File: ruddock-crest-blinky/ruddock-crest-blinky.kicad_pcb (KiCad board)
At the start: 2 copper layers, 38.1 x 45.7 mm, 38 parts, among them J1 JST PH, Q1 IRFML8244, SW1 JS102011JCQN, SW2 PTS 647 SK38 SMTR2 LFS, U1 ATtiny85-20SU, U2 74HC595

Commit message: Begin layout
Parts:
- removed the G*** at (141.0, 108.2)
- removed H1: BAT_POS, TestPoint:TestPoint_Pad_4.0x4.0mm
- removed H2: BAT_NEG, TestPoint:TestPoint_Pad_4.0x4.0mm
- removed the R1 at (108.5, 105.3)
- added BT1: 3024, Battery:BatteryHolder_Keystone_3034_1x20mm, B.Cu at (212.1, 79.0)
- added C5: 1uF, Capacitor_SMD:C_0805_2012Metric_Pad1.15x1.40mm_HandSolder, B.Cu at (198.1, 59.4)
- added R10: 10K, Resistor_SMD:R_0805_2012Metric_Pad1.15x1.40mm_HandSolder, B.Cu at (207.5, 54.6)
- added R9: 10K, Resistor_SMD:R_0805_2012Metric_Pad1.15x1.40mm_HandSolder, B.Cu at (201.9, 67.3)
- added U3: AP7370-50, Package_TO_SOT_SMD:SOT-89-3_Handsoldering, B.Cu at (194.3, 63.2)
- C1, C2, C3, C4, F1, J1, Q1, SW2, U1, U2: moved to B.Cu
- C6: renamed from C5; value 1uF -> 0.1uF; moved to B.Cu
- moved J1 134.7 mm to (212.1, 85.1), turned to 0 degrees
- moved Q1 134.2 mm to (226.1, 71.1), turned to 90 degrees
- moved C1 123.1 mm to (204.0, 54.6), turned to 90 degrees
- moved SW2 118.2 mm to (176.5, 55.9)
- moved U1 114.2 mm to (205.7, 61.0)
- moved U2 113.4 mm to (217.2, 59.7)
- moved C2 111.3 mm to (210.8, 54.6), turned to 90 degrees
- moved C6 106.6 mm to (200.7, 54.6), turned to 90 degrees
- moved F1 98.4 mm to (196.8, 79.0), turned to 90 degrees
- moved C4 94.8 mm to (193.8, 69.4)
- moved C3 86.7 mm to (193.8, 72.9)
- moved G*** 52.2 mm to (106.7, 147.3)
- moved G*** 43.2 mm to (184.2, 106.7)
- moved R11 4.72 mm to (129.8, 74.5)
- renumbered R2 to R1, R10 to R11, R3 to R2, R4 to R3, R5 to R4, R6 to R5, R7 to R6, R8 to R7, R9 to R8
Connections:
- net Net-(R2-Pad1) renamed /LED1
- net Net-(R3-Pad1) renamed /LED2
- net Net-(R4-Pad1) renamed /LED3
- net Net-(R5-Pad1) renamed /LED4
- net Net-(R6-Pad1) renamed /LED5
- net Net-(R7-Pad1) renamed /LED6
- net Net-(R8-Pad1) renamed /LED7
- net Net-(R9-Pad1) renamed /LED8
- C1 pad 1: VCC -> VDD
- C2 pad 1: GND -> VDD
- C2 pad 2: VCC -> GND
- C3 pad 1: VCC -> +BATT
- C4 pad 1: VCC -> +BATT
- Q1 pad 1: VCC -> +BATT
- R11 pad 1: VCC -> VDD
- SW1 pad 2: VCC -> +BATT
- U1 pad 8: VCC -> VDD
- U2 pad 10: VCC -> VDD
- U2 pad 16: VCC -> VDD
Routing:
- net Net-(R2-Pad2): track 21.2 -> 0.00 mm
- net VDD: track 0.00 -> 5.31 mm
- net /SER: track 26.9 -> 25.1 mm
- net /RCLK: track 6.58 -> 5.31 mm
- net /~OE: track 6.58 -> 6.05 mm
- net /SRCLK: track 6.58 -> 6.05 mm
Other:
- net class Power added: clearance 0.381, trace_width 0.762, via_dia 1.016, via_drill 0.508

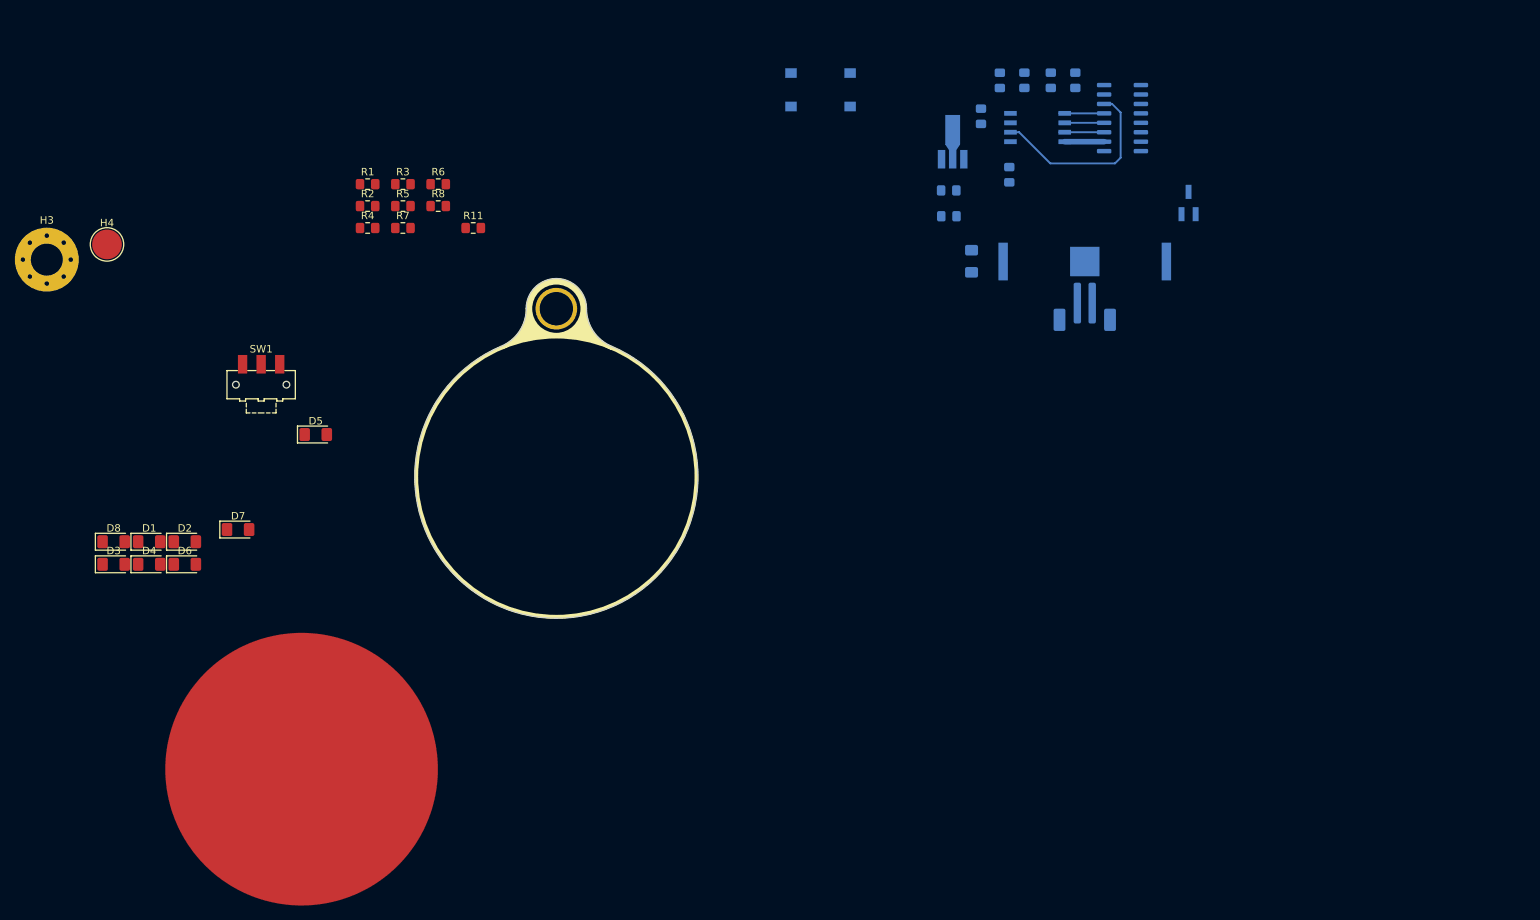
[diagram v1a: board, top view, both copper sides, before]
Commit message: Remove dual cell and JST option, continue design
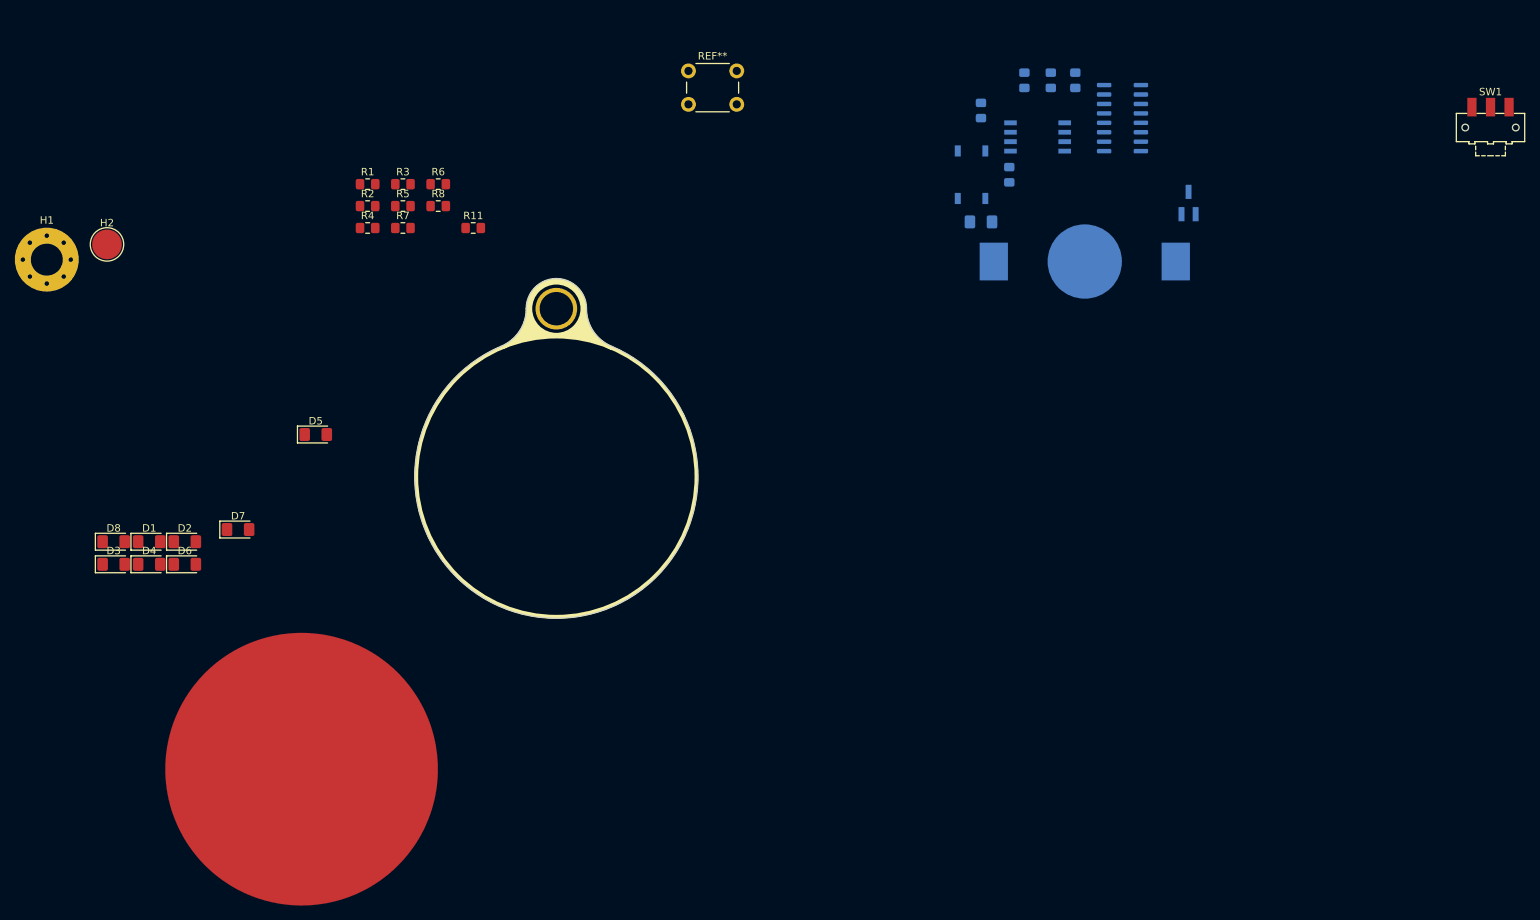
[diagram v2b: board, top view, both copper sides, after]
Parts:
- removed the C3 at (193.8, 72.9)
- removed C4, C5: 1uF, Capacitor_SMD:C_0805_2012Metric_Pad1.15x1.40mm_HandSolder
- removed J1: JST PH, Connector_JST:JST_PH_B2B-PH-SM4-TB_1x02-1MP_P2.00mm_Vertical
- removed U3: AP7370-50, Package_TO_SOT_SMD:SOT-89-3_Handsoldering
- added REF**: SW_PUSH_6mm, Button_Switch_THT:SW_PUSH_6mm, F.Cu at (158.8, 53.3)
- BT1: value 3024 -> 3034; footprint Battery:BatteryHolder_Keystone_3034_1x20mm -> ruddock-crest-blinky:BatteryHolder_Keystone_3034_Wide
- SW2: value PTS 647 SK38 SMTR2 LFS -> PTS526 SK15 SMTR2 LFS; footprint Button_Switch_SMD:SW_SPST_PTS645 -> ruddock-crest-blinky:SW_SPST_PTS526
- moved SW1 169.0 mm to (266.7, 61.0)
- moved SW2 23.3 mm to (196.8, 67.3), turned to 90 degrees
- moved F1 5.45 mm to (198.1, 73.7), turned to 0 degrees
- moved C3 4.78 mm to (198.1, 58.7)
- moved U1 1.27 mm to (205.7, 62.2)
- renumbered C6 to C3, H3 to H1, H4 to H2
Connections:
- Q1 pad 1: +BATT -> VDD
- SW1 pad 2: +BATT -> VDD
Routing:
- net /SER: track 25.1 -> 0.00 mm
- net /SRCLK: track 6.05 -> 0.00 mm
- net /~OE: track 6.05 -> 0.53 mm
- net VDD: track 5.31 -> 0.00 mm
- net /RCLK: track 5.31 -> 0.00 mm

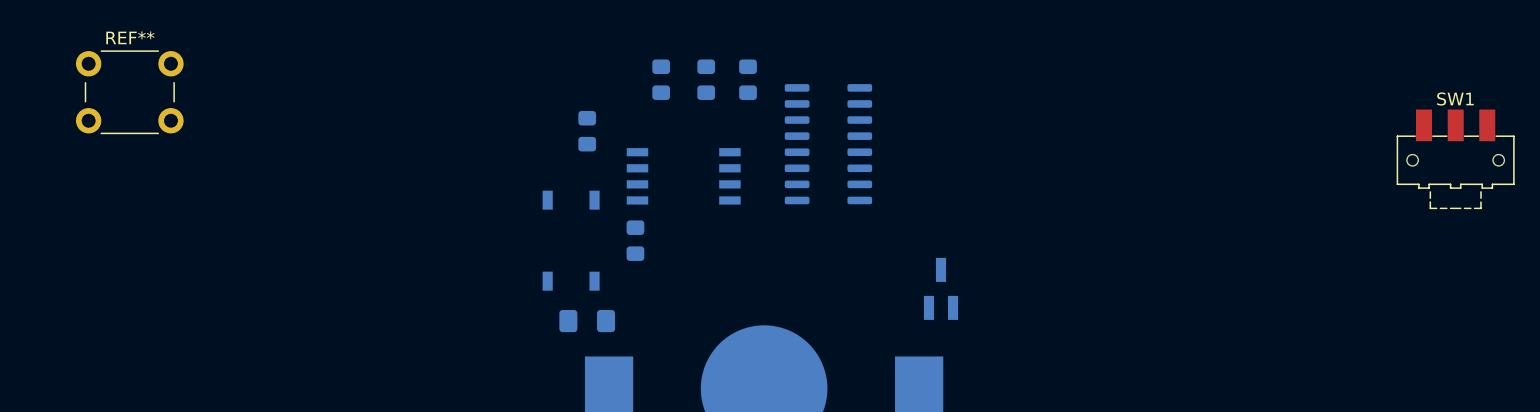
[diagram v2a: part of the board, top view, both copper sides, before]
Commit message: Update power switch
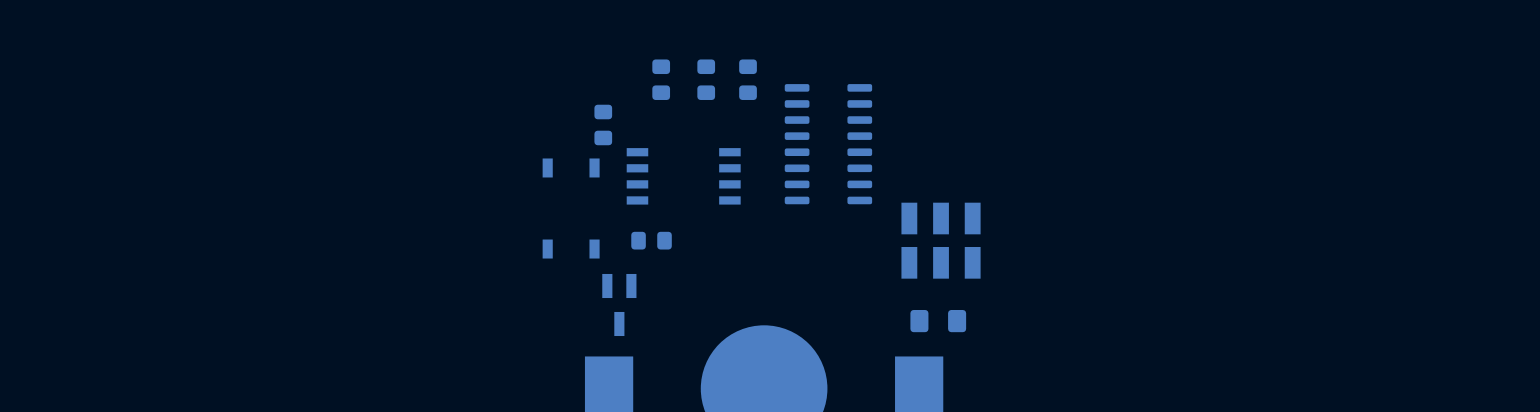
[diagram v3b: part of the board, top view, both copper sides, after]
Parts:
- removed the REF** at (158.8, 53.3)
- SW1: value JS102011JCQN -> JS202011JCQN; footprint Button_Switch_SMD:SW_SPDT_CK-JS102011SAQN -> ruddock-crest-blinky:SW_SPDT_CK-JS202011JCQN; moved to B.Cu
- moved SW1 41.1 mm to (226.1, 67.3)
- moved F1 27.7 mm to (225.8, 73.7)
- moved Q1 25.4 mm to (200.7, 72.4), turned to 270 degrees
- moved SW2 2.54 mm to (196.8, 64.8)
- moved C3 1.36 mm to (199.4, 58.2)
- moved R9 1.27 mm to (203.2, 67.3), turned to 180 degrees

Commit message: Continue placement
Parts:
- removed C2: 0.1uF, Capacitor_SMD:C_0805_2012Metric_Pad1.15x1.40mm_HandSolder
- R1, R11, R2, R3, R4, R5, R6, R7, R8: moved to B.Cu
- moved D1 115.1 mm to (177.8, 47.0), turned to 180 degrees
- moved R4 111.2 mm to (225.4, 57.1), turned to 90 degrees
- moved R2 106.5 mm to (220.3, 52.7)
- moved R5 104.4 mm to (224.2, 61.0)
- moved R3 103.3 mm to (222.9, 55.9), turned to 90 degrees
- moved R1 99.6 mm to (214.0, 53.3), turned to 180 degrees
- moved R6 94.0 mm to (219.1, 67.3), turned to 180 degrees
- moved R7 91.4 mm to (209.6, 54.6), turned to 180 degrees
- moved R8 85.0 mm to (207.6, 51.4), turned to 180 degrees
- moved R11 77.3 mm to (204.5, 54.6), turned to 180 degrees
- moved R10 3.78 mm to (209.6, 57.8), turned to 180 degrees
- moved C1 3.22 mm to (204.5, 57.8), turned to 180 degrees
- moved Q1 2.84 mm to (198.1, 71.1), turned to 0 degrees
- moved F1 1.42 mm to (227.1, 73.0)
- moved U1 0.90 mm to (206.4, 62.9)
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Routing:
- net /~OE: track 0.53 -> 9.20 mm
- net /SRCLK: track 0.00 -> 5.13 mm
- net VDD: track 0.00 -> 5.13 mm
- net /RCLK: track 0.00 -> 5.13 mm
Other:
- board text added: "RuddBlink"
- board text added: "Virtutis mammilas exsugimus"
- board text added: "v0.1"

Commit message: Finish placement
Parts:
- moved D3 153.3 mm to (228.1, 75.2), turned to 67.5 degrees
- moved D2 147.6 mm to (228.1, 62.0), turned to 112.5 degrees
- moved D8 139.7 mm to (205.5, 52.6), turned to 202.5 degrees
- moved D4 137.1 mm to (218.7, 84.6), turned to 22.5 degrees
- moved D6 114.2 mm to (196.1, 75.2), turned to 292.5 degrees
- moved D7 111.4 mm to (196.1, 62.0), turned to 247.5 degrees
- moved D5 98.5 mm to (205.5, 84.6), turned to 337.5 degrees
- moved G*** 52.2 mm to (141.0, 108.0)
- moved G*** 43.2 mm to (141.0, 108.0)
- moved D1 41.3 mm to (218.7, 52.6), turned to 157.5 degrees
- moved R6 9.66 mm to (227.0, 61.7), turned to 0 degrees
- moved R8 3.42 mm to (208.9, 54.6)
- moved R7 3.24 mm to (208.9, 51.4)
- moved R5 1.70 mm to (223.0, 59.7), turned to 270 degrees
- moved R2 1.21 mm to (219.2, 52.3)
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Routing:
- net /LED8: track 0.00 -> 15.3 mm
- net /LED7: track 0.00 -> 13.6 mm
- net /USER: track 0.00 -> 9.03 mm
- net /LED1: track 0.00 -> 7.45 mm
- net /~OE: track 9.20 -> 5.13 mm
- net /LED4: track 0.00 -> 0.83 mm
